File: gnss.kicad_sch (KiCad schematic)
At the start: 72 parts, among them J11 Conn_Coaxial, J12 Conn_Coaxial_Small, Q12 AO3401A, Q13 BSS138, SW4 RESET_GNSS, SW5 SAFEBOOT_GNSS, U10 TPS7A2033PDBVR, U11 TPS259474LRPWR, U9 NEO-M9N

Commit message: add photos to journal
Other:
- note added: "High to enable I2C/UART, low to enable SPI Only for NEO-M(#)N"
- note removed: "High to enable I2C/UART, low to enable SPI"
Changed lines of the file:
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@@
 		)
 	)
-	(text "High to enable I2C/UART, low to enable SPI"
+	(text "High to enable I2C/UART, low to enable SPI\nOnly for NEO-M(#)N"
 		(exclude_from_sim no)
 		(at 47.752 28.448 0)

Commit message: actually better routing this time
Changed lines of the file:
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@@
 	(wire
 		(pts
-			(xy 153.67 144.78) (xy 154.94 144.78)
+			(xy 153.67 144.78) (xy 158.75 144.78)
 		)
 		(stroke
@@
 	(global_label "GPS_ANT"
 		(shape bidirectional)
-		(at 154.94 144.78 0)
+		(at 158.75 144.78 0)
 		(fields_autoplaced yes)
 		(effects
@@
 		)
 		(property "Intersheetrefs" "${INTERSHEET_REFS}"
-			(at 167.1403 144.78 0)
+			(at 170.9503 144.78 0)
 			(hide yes)
 			(show_name no)

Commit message: new part numbers for out of stock components
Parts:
- C110: LCSC Part C7393892 -> C22392391
- C96, C97: LCSC Part (none) -> C696856
- R89: LCSC Part C4354980 -> C723682
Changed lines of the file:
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@@
 			)
 		)
-		(property "LCSC Part" "C4354980"
+		(property "LCSC Part" "C723682"
 			(at 257.81 66.04 0)
 			(hide yes)
@@
 			)
 		)
+		(property "Capacitor Rating" ""
+			(at 257.81 66.04 0)
+			(hide yes)
+			(show_name no)
+			(do_not_autoplace no)
+			(effects
+				(font
+					(size 1.27 1.27)
+				)
+			)
+		)
 		(pin "1"
 		)
@@
 			)
 		)
-		(property "LCSC Part" ""
+		(property "LCSC Part" "C696856"
 			(at 85.09 149.86 0)
 			(hide yes)
@@
 			)
 		)
+		(property "Capacitor Rating" ""
+			(at 85.09 149.86 0)
+			(hide yes)
+			(show_name no)
+			(do_not_autoplace no)
+			(effects
+				(font
+					(size 1.27 1.27)
+				)
+			)
+		)
 		(pin "1"
 		)
@@
 		)
 		(property "Value" "DISABLE_GNSS_PROT"
-			(at 266.7 95.504 0)
+			(at 266.446 95.504 0)
 			(show_name no)
 			(do_not_autoplace no)
@@
 		(dnp no)
 		(property "Reference" "C111"
-			(at 264.922 77.724 90)
+			(at 270.002 76.2 90)
 			(show_name no)
 			(do_not_autoplace no)
@@
 		)
 		(property "Value" "10uF"
-			(at 264.668 74.168 90)
+			(at 264.414 73.66 90)
 			(show_name no)
 			(do_not_autoplace no)
@@
 			)
 		)
-		(property "LCSC Part" ""
+		(property "LCSC Part" "C696856"
 			(at 69.85 149.86 0)
 			(hide yes)
@@
 			)
 		)
+		(property "Capacitor Rating" ""
+			(at 69.85 149.86 0)
+			(hide yes)
+			(show_name no)
+			(do_not_autoplace no)
+			(effects
+				(font
+					(size 1.27 1.27)
+				)
+			)
+		)
 		(pin "1"
 		)
@@
 		(dnp no)
 		(property "Reference" "C110"
-			(at 264.414 69.85 90)
+			(at 270.002 71.12 90)
 			(show_name no)
 			(do_not_autoplace no)
@@
 			)
 		)
-		(property "LCSC Part" "C7393892"
+		(property "LCSC Part" "C22392391"
 			(at 261.62 71.12 0)
 			(hide yes)
@@
 			(hide yes)
 			(show_name no)
+			(do_not_autoplace no)
+			(effects
+				(font
+					(size 1.27 1.27)
+				)
+			)
+		)
+		(property "Capacitor Rating" ""
+			(at 261.62 71.12 0)
+			(hide yes)
+			(show_name no)

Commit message: backup before switching to kicad-nightly
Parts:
- J11: value Conn_Coaxial -> XUNPU SMA-KE-347-H13.5-1.6; LCSC Part C5250058 -> C5723200
- U9: value NEO-M9N -> NEO-F10N; LCSC Part C5119087 -> (none); now in the parts list
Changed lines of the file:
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@@
 		(body_style 1)
 		(exclude_from_sim no)
-		(in_bom no)
+		(in_bom yes)
 		(on_board yes)
 		(in_pos_files yes)
@@
 			)
 		)
-		(property "Value" "NEO-M9N"
+		(property "Value" "NEO-F10N"
 			(at 106.426 42.926 0)
 			(show_name no)
@@
 			)
 		)
-		(property "Datasheet" "https://content.u-blox.com/sites/default/files/NEO-M9N_Integrationmanual_UBX-19014286.pdf"
+		(property "Datasheet" "https://content.u-blox.com/sites/default/files/documents/NEO-F10N_DataSheet_UBX-23002117.pdf"
 			(at 120.396 104.902 0)
 			(hide yes)
@@
 			)
 		)
-		(property "Description" "GNSS Module NEO M8, VCC 2.7V to 3.6V"
+		(property "Description" "u-blox F10 standard precision GNSS module"
 			(at 124.206 27.94 0)
 			(hide yes)
@@
 			)
 		)
-		(property "LCSC Part" "C5119087"
-			(at 147.574 90.17 0)
-			(hide yes)
-			(show_name no)
-			(do_not_autoplace no)
-			(effects
-				(font
-					(size 1.27 1.27)
-				)
-			)
-		)
 		(property "Voltage Rating" ""
 			(at 121.92 69.85 0)
@@
 			)
 		)
-		(property "KLC_S3.3" ""
+		(property "Capacitor Rating" ""
 			(at 121.92 69.85 0)
 			(hide yes)
@@
 			)
 		)
-		(property "KLC_S5.1" ""
+		(property "LCSC Part" ""
 			(at 121.92 69.85 0)
 			(hide yes)
@@
 			)
 		)
-		(property "Value" "Conn_Coaxial"
+		(property "Value" "XUNPU SMA-KE-347-H13.5-1.6"
 			(at 35.8532 124.46 90)
 			(hide yes)
@@
 			)
 		)
-		(property "LCSC Part" "C5250058"
+		(property "LCSC Part" "C5723200"
 			(at 35.56 128.27 0)
 			(hide yes)

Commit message: lots of fixes!
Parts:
- L2: LCSC Part C98077 -> C98076; MPN (none) -> LQW18AN47NG00D
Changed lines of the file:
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@@
 (kicad_sch
-	(version 20260306)
+	(version 20260830)
 	(generator "eeschema")
-	(generator_version "10.0")
+	(generator_version "10.99")
 	(paper "A4")
 	(title_block
@@
 			)
 		)
-		(property "LCSC Part" "C98077"
+		(property "LCSC Part" "C98076"
 			(at 35.56 149.86 0)
 			(hide yes)
@@
 			)
 		)
-		(property "LCSC" ""
+		(property "KLC_S3.3" ""
 			(at 35.56 149.86 0)
 			(hide yes)
@@
 			)
 		)
-		(property "KLC_S3.3" ""
+		(property "KLC_S5.1" ""
 			(at 35.56 149.86 0)
 			(hide yes)
@@
 			)
 		)
-		(property "KLC_S5.1" ""
+		(property "MPN" "LQW18AN47NG00D"
 			(at 35.56 149.86 0)
 			(hide yes)

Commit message: organize part fields
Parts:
- BT3: MPN (none) -> MS621FE-FL11E; Manufacturer (none) -> Seiko Instruments
- C100, C102, C103, C106, C107, C111, C130, C99: Dielectric (none) -> X5R; MPN (none) -> CGA0402X5R106M100GT; Manufacturer (none) -> HRE; Tolerance (none) -> 20%; Voltage Rating (none) -> 10V
- C101: Dielectric (none) -> X5R; MPN (none) -> CGA0402X5R475M250GT; Manufacturer (none) -> HRE; Tolerance (none) -> 20%; Voltage Rating (none) -> 25V
- C104: Dielectric (none) -> X5R; MPN (none) -> HGC0402R5225K350NTEJ; Manufacturer (none) -> Chinocera; Tolerance (none) -> 10%; Voltage Rating 16V -> 35V
- C108: Dielectric (none) -> C0G; MPN (none) -> GRM1555C1H222GA01D; Manufacturer (none) -> Murata; Tolerance (none) -> 2%; Voltage Rating (none) -> 50V
- C109: Capacitor Rating C0G -> (none); Dielectric (none) -> C0G; MPN (none) -> GRM1555C1H222GA01D; Manufacturer (none) -> Murata; Tolerance (none) -> 2%; Voltage Rating (none) -> 50V
- C110: Dielectric (none) -> X5R; MPN (none) -> TCC0603X5R106M350CT; Manufacturer (none) -> CCTC; Tolerance (none) -> 20%; Voltage Rating (none) -> 35V
- C93: Capacitor Rating C0G/NP0 -> (none); Dielectric (none) -> C0G; MPN (none) -> TCC0402COG220J500AT; Manufacturer (none) -> CCTC; Tolerance (none) -> 5%; Voltage Rating 25V -> 50V
- C94: Capacitor Rating X7R -> (none); Dielectric (none) -> X7R; MPN (none) -> TCC0402X7R105K250AT; Manufacturer (none) -> CCTC; Tolerance (none) -> 10%; Voltage Rating 16V -> 25V
- C95: Capacitor Rating C0G/NP0 -> (none); Dielectric (none) -> C0G; MPN (none) -> CGA0402C0G470J500GT; Manufacturer (none) -> HRE; Tolerance (none) -> 5%; Voltage Rating 25V -> 50V
- C96, C97: Dielectric (none) -> X7R; MPN (none) -> TCC0402X7R103M500AT; Manufacturer (none) -> CCTC; Tolerance (none) -> 20%; Voltage Rating (none) -> 50V
- D10, D13: MPN (none) -> ESD501DPYR; Manufacturer (none) -> Texas Instruments
- D11: MPN (none) -> GL0805UR01; Manufacturer (none) -> Guiguang
- D12: MPN (none) -> GL0805UB01; Manufacturer (none) -> Guiguang
- D14: MPN (none) -> ESD351DPYR; Manufacturer (none) -> Texas Instruments
- D15, D16: MPN (none) -> RB531SM-30T2R; Manufacturer (none) -> ROHM
- D17: MPN (none) -> TPD1E10B06DPYR; Manufacturer (none) -> Texas Instruments
- FB1: MPN (none) -> BLM18HG601SN1D; Manufacturer (none) -> Murata
- FL1: MPN (none) -> B39162B8389P810; Manufacturer (none) -> Qualcomm (RF360)
- J11: value XUNPU SMA-KE-347-H13.5-1.6 -> SMA-KE-347-H13.5-1.6; MPN (none) -> SMA-KE-347-H13.5-1.6; Manufacturer (none) -> XUNPU
- J12: value Conn_Coaxial_Small -> U.FL; MPN (none) -> U.FL-R-SMT-1(80); Manufacturer (none) -> Hirose
- JP10: private KLC_S3.3 -> (none)
- L2: Manufacturer (none) -> Murata; Note (none) -> SRF >= 2GHz; Tolerance (none) -> 2%
- L6, L7: MPN (none) -> MLG1005S5N1CTD25; Manufacturer (none) -> TDK; Note (none) -> Q=42 @ 1.8GHz
- Q12: MPN (none) -> AO3401A; Manufacturer (none) -> UMW
- Q13: MPN (none) -> BSS138; Manufacturer (none) -> KUU
- R134, R69, R73, R75: MPN (none) -> CRCW04020000Z0EDHP; Manufacturer (none) -> Vishay
- R67, R76: MPN (none) -> FRH0402D1002TS; Manufacturer (none) -> FOJAN; Power Rating (none) -> 62.5mW; Tolerance (none) -> 0.5%
- R68, R72: MPN (none) -> TC0225B2201TCC; Manufacturer (none) -> UNI-ROYAL; Power Rating (none) -> 62.5mW; Tolerance (none) -> 0.1%
- R70: MPN (none) -> TC0225B2001TCC; Manufacturer (none) -> UNI-ROYAL; Power Rating (none) -> 62.5mW; Tolerance (none) -> 0.1%
- R71, R78: MPN (none) -> FRH0402B1001TS; Manufacturer (none) -> FOJAN; Power Rating (none) -> 62.5mW; Tolerance (none) -> 0.1%
- R74: MPN (none) -> AS05W2J0620T5E; Manufacturer (none) -> UNI-ROYAL; Tolerance (none) -> 5%
- R77, R79, R91: MPN (none) -> ARG02BTC1003; Manufacturer (none) -> Viking Tech; Power Rating (none) -> 62.5mW; Tolerance (none) -> 0.1%
- R80, R83: MPN (none) -> AR02DTC1500; Manufacturer (none) -> Viking Tech; Power Rating (none) -> 62.5mW; Tolerance 1% -> 0.5%
- R81: MPN (none) -> RK73H1ETTP37R4F; Manufacturer (none) -> KOA Speer; Power Rating (none) -> 100mW
- R82: MPN (none) -> AR02BTC4701; Manufacturer (none) -> Viking Tech; Power Rating (none) -> 62.5mW; Tolerance (none) -> 0.1%
- R84: MPN (none) -> AR02BTC1503; Manufacturer (none) -> Viking Tech; Power Rating (none) -> 62.5mW; Tolerance 0.5% -> 0.1%
- R85: MPN (none) -> RT0603BRD07215KL; Manufacturer (none) -> YAGEO; Power Rating (none) -> 100mW
- R86: MPN (none) -> ARG02BTC1003; Manufacturer (none) -> Viking Tech; Power Rating (none) -> 62.5mW; Tolerance 0.5% -> 0.1%
- R87: MPN (none) -> ARG02BTC1133; Manufacturer (none) -> Viking Tech; Power Rating (none) -> 62.5mW
- R88: MPN (none) -> GR0402F6K65TAG00; Manufacturer (none) -> GiantOhm; Power Rating (none) -> 62.5mW
- R89: MPN (none) -> AT0603BRD07200KL; Manufacturer (none) -> YAGEO; Power Rating (none) -> 100mW; Tolerance 1% -> 0.1%
- R90: MPN (none) -> RE0402BRE07301KL; Manufacturer (none) -> YAGEO; Power Rating (none) -> 62.5mW; Tolerance (none) -> 0.1%
- SW4, SW5: MPN (none) -> SKRKAHE020; Manufacturer (none) -> Alps Alpine
- U10, U11: Manufacturer TI(德州仪器) -> Texas Instruments
- U9: LCSC Part (none) -> C21709333; MPN (none) -> NEO-F10N-00B; Manufacturer (none) -> u-blox

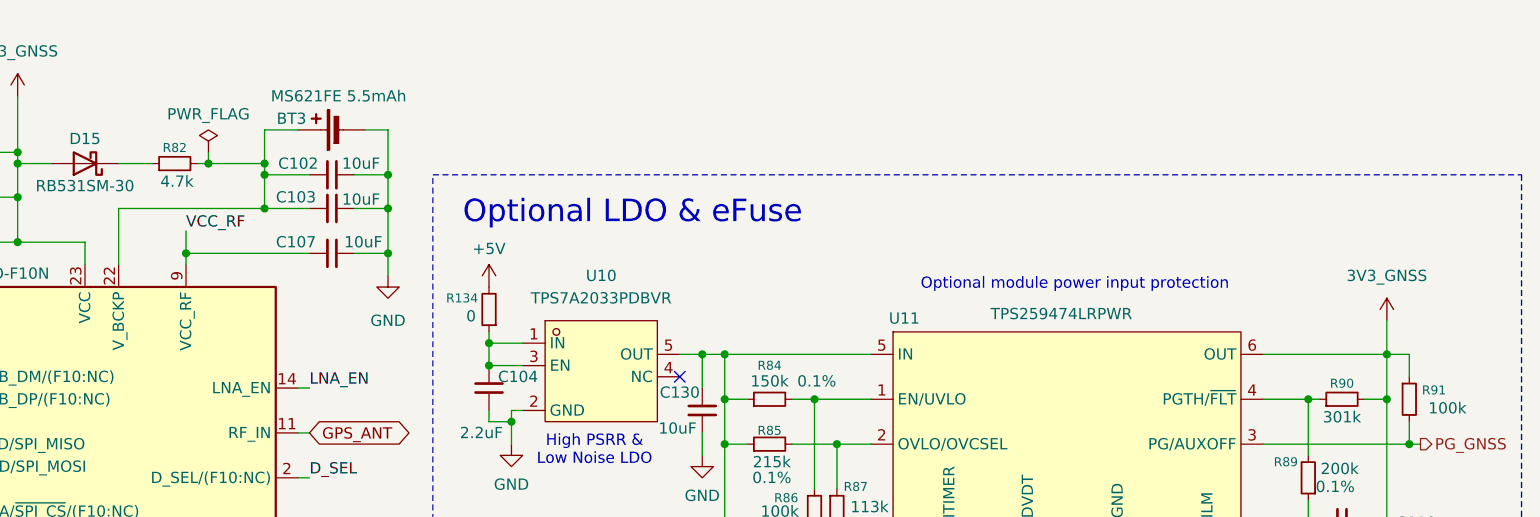
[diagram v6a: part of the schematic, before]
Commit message: add extra PWR_FLAGs
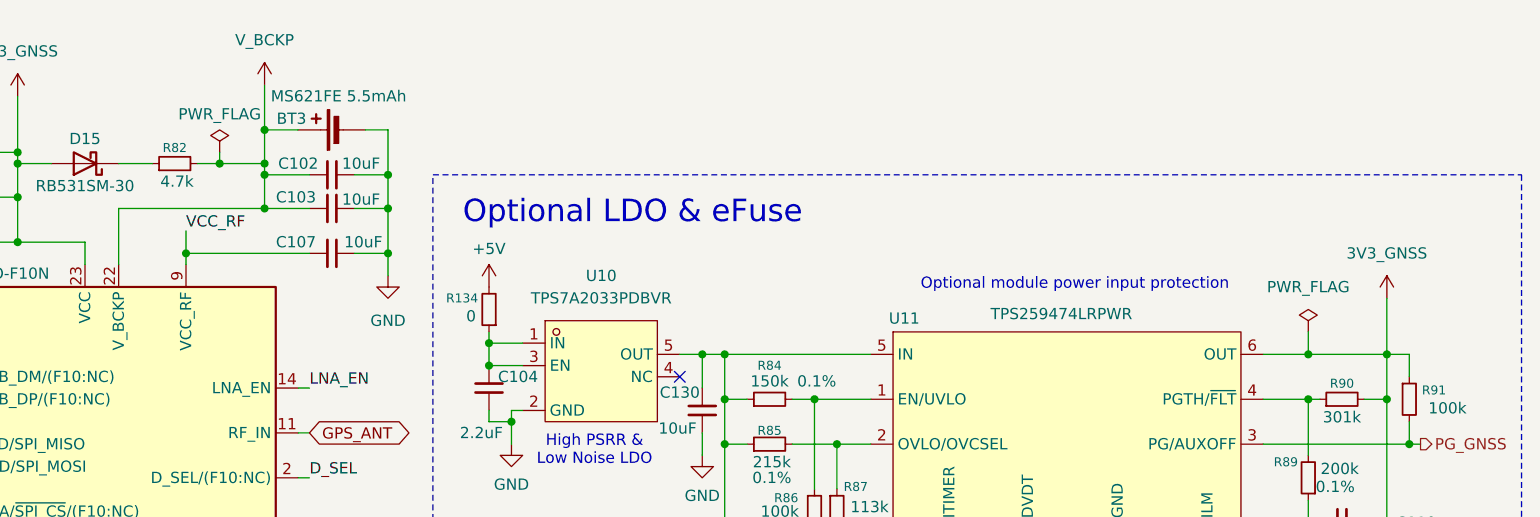
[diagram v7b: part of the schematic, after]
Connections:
- net V_BCKP: now reaches BT3.1 (+), C102.2, C103.2, R82.2, U9.22 (V_BCKP)

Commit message: nearly set to order!
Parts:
- BT3: now in the parts list
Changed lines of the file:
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@@
 		(body_style 1)
 		(exclude_from_sim no)
-		(in_bom no)
+		(in_bom yes)
 		(on_board yes)
 		(in_pos_files yes)
@@
 			(at 148.59 26.67 0)
 			(hide yes)
+			(show_name no)
+			(do_not_autoplace no)
+			(effects
+				(font
+					(size 1.27 1.27)
+				)
+			)
+		)
+		(property "LCSC Part" ""
+			(at 148.59 26.67 0)
+			(hide yes)
+			(show_name no)
+			(do_not_autoplace no)
+			(effects
+				(font
+					(size 1.27 1.27)
+				)
+			)
+		)
+		(property "Voltage Rating" ""
+			(at 148.59 26.67 0)
+			(hide yes)
+			(show_name no)
+			(do_not_autoplace no)
+			(effects
+				(font
+					(size 1.27 1.27)
+				)
+			)
+		)
+		(property "Tolerance" ""
+			(at 148.59 26.67 0)
+			(hide yes)
